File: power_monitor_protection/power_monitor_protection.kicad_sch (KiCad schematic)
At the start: 10 parts, among them J1 Conn_01x05_Socket, J2 Conn_01x04_Socket, U1 ADuM1201AR, U3 B0503S-1WR3

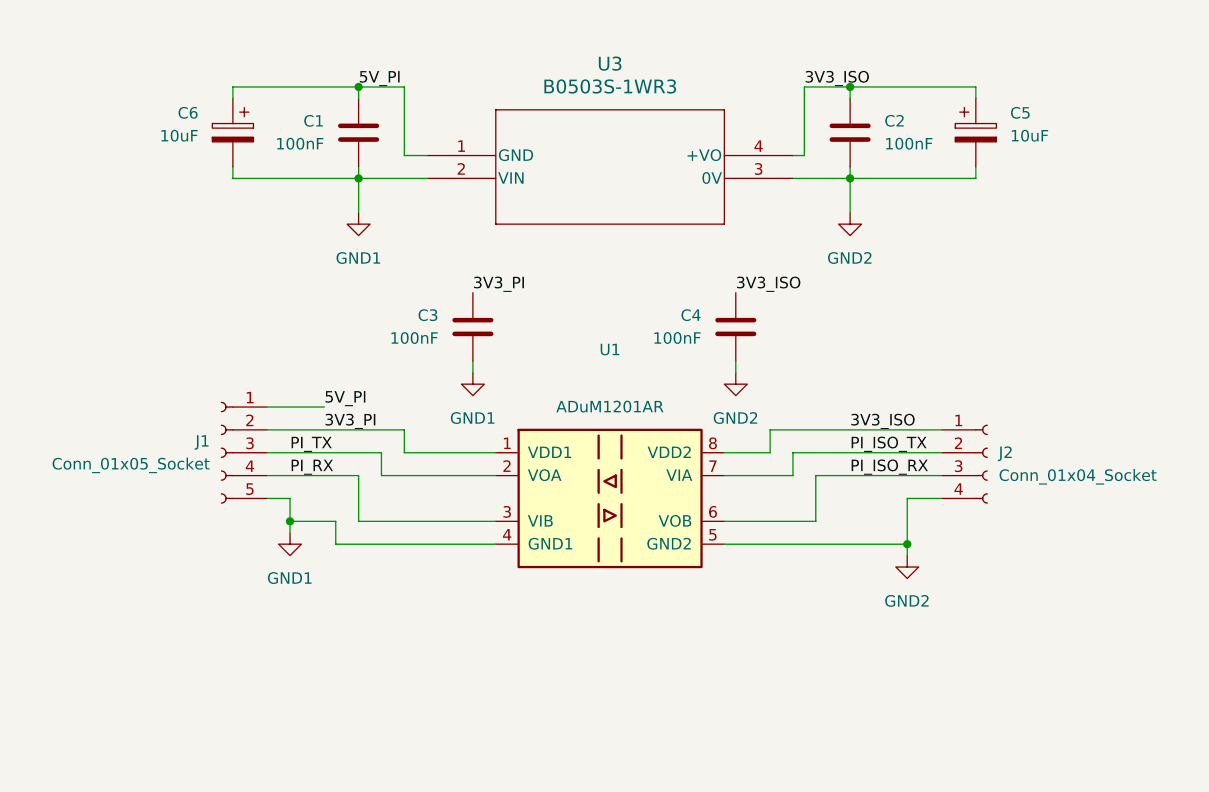
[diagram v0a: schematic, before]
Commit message: fix: erc issues with power monitor protection
Signed-off-by: Scott Gibb <smgibb@yahoo.com>
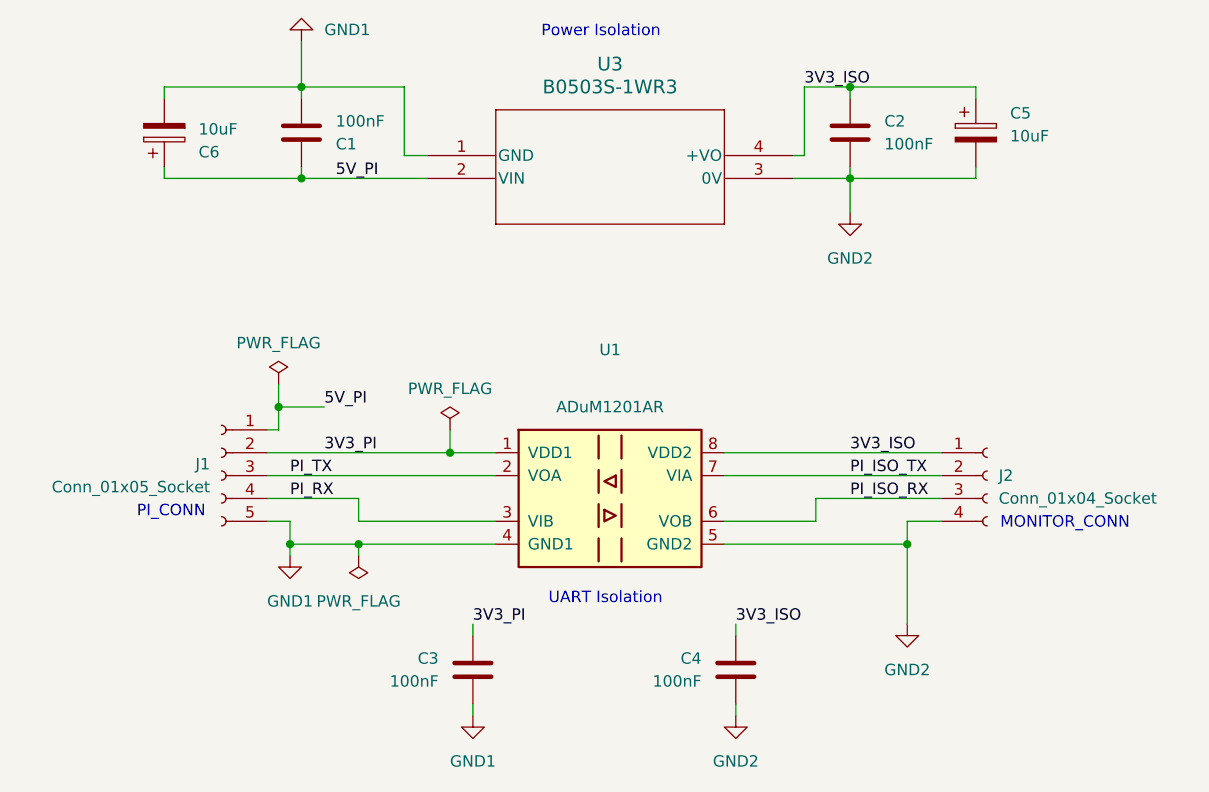
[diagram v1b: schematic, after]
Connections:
- net 5V_PI: now also U3.2 (VIN); no longer U3.1 (GND)
- net GND1: now also U3.1 (GND); no longer U3.2 (VIN)
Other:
- note added: "MONITOR_CONN"
- note added: "PI_CONN"
- note added: "Power Isolation"
- note added: "UART Isolation"
- title: (none) -> Power Monitor Isolation
- moved on the sheet: C1, C3, C4, C6, J1, J2

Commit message: fic: erc rules
Signed-off-by: Scott Gibb <smgibb@yahoo.com>
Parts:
- U3: footprint SIP4_B_S-1WR3_MNS -> DCDC:SIP4_B_S-1WR3_MNS
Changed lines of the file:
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@@
 			)
 		)
-		(property "Footprint" "SIP4_B_S-1WR3_MNS"
+		(property "Footprint" "DCDC:SIP4_B_S-1WR3_MNS"
 			(at 80.01 38.1 0)
 			(hide yes)

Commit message: fix: schematic and footprint symbols
Signed-off-by: Scott Gibb <smgibb@yahoo.com>
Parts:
- U3: symbol 2026-06-24_20-18-09:B0505S-1WR3 -> DCDC:B0505S-1WR3
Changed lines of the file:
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@@
 	)
 	(symbol
-		(lib_id "2026-06-24_20-18-09:B0505S-1WR3")
+		(lib_id "DCDC:B0505S-1WR3")
 		(at 80.01 38.1 0)
 		(unit 1)

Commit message: fix(protection): correct UART labels for isolator direction
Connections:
- net PI_ISO_RX: now also J2.2 (Pin_2), U1.7 (VIA); no longer J2.3 (Pin_3), U1.6 (VOB)
- net PI_ISO_TX: now also J2.3 (Pin_3), U1.6 (VOB); no longer J2.2 (Pin_2), U1.7 (VIA)
- net PI_RX: now also J1.3 (Pin_3), U1.2 (VOA); no longer J1.4 (Pin_4), U1.3 (VIB)
- net PI_TX: now also J1.4 (Pin_4), U1.3 (VIB); no longer J1.3 (Pin_3), U1.2 (VOA)
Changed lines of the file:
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@@
 		)
 	)
-	(label "PI_RX"
+	(label "PI_TX"
 		(at 64.77 76.2 0)
 		(effects
@@
 		)
 	)
-	(label "PI_ISO_RX"
+	(label "PI_ISO_TX"
 		(at 127 76.2 0)
 		(effects
@@
 		)
 	)
-	(label "PI_TX"
+	(label "PI_RX"
 		(at 64.77 73.66 0)
 		(effects
@@
 		)
 	)
-	(label "PI_ISO_TX"
+	(label "PI_ISO_RX"
 		(at 127 73.66 0)
 		(effects
